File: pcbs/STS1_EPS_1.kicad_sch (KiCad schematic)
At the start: 4 parts, among them J1 Inter-EPS, U12 BD50GA5WEFJ

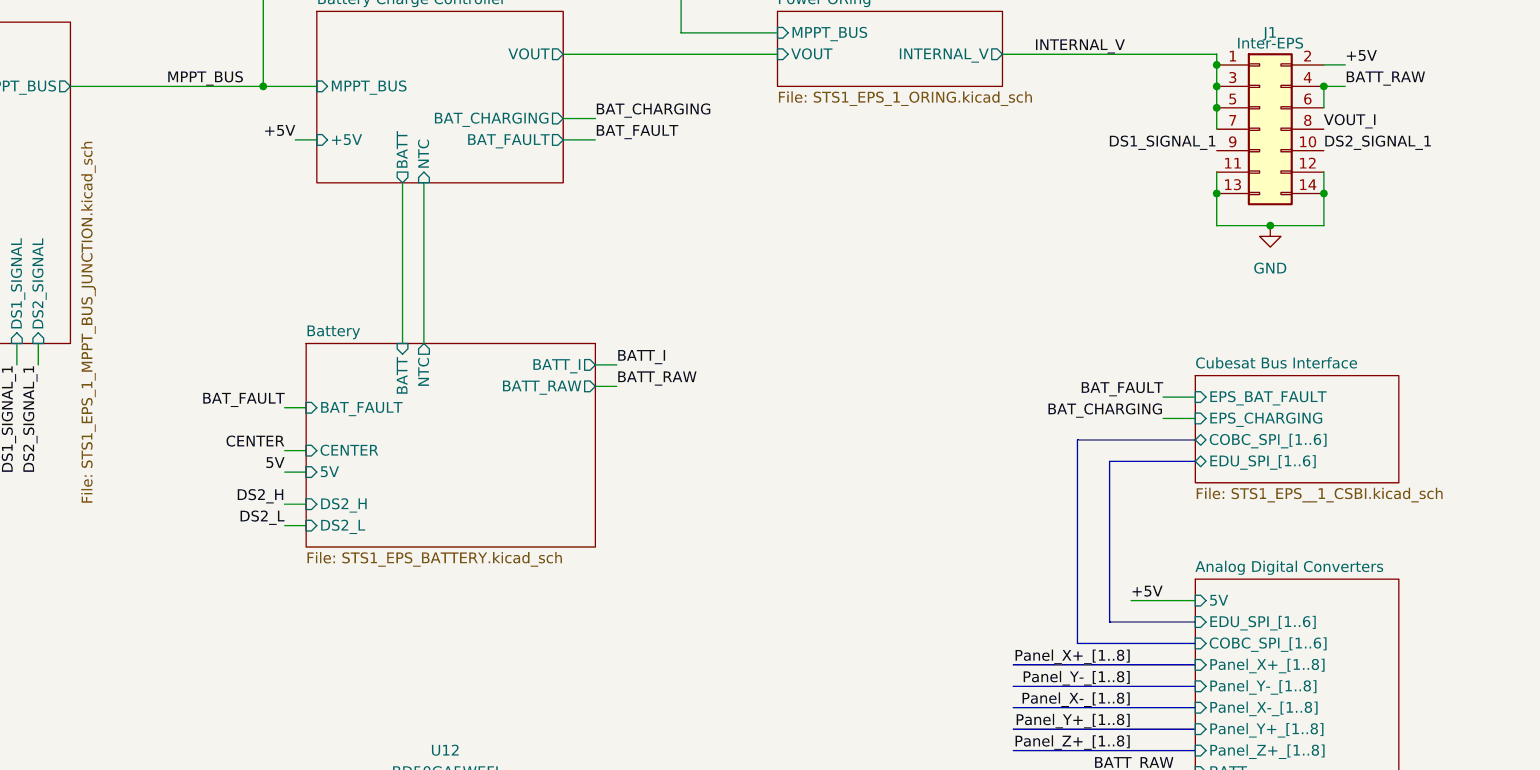
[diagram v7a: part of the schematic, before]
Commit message: Worked on STS1_EPS_2 layout.
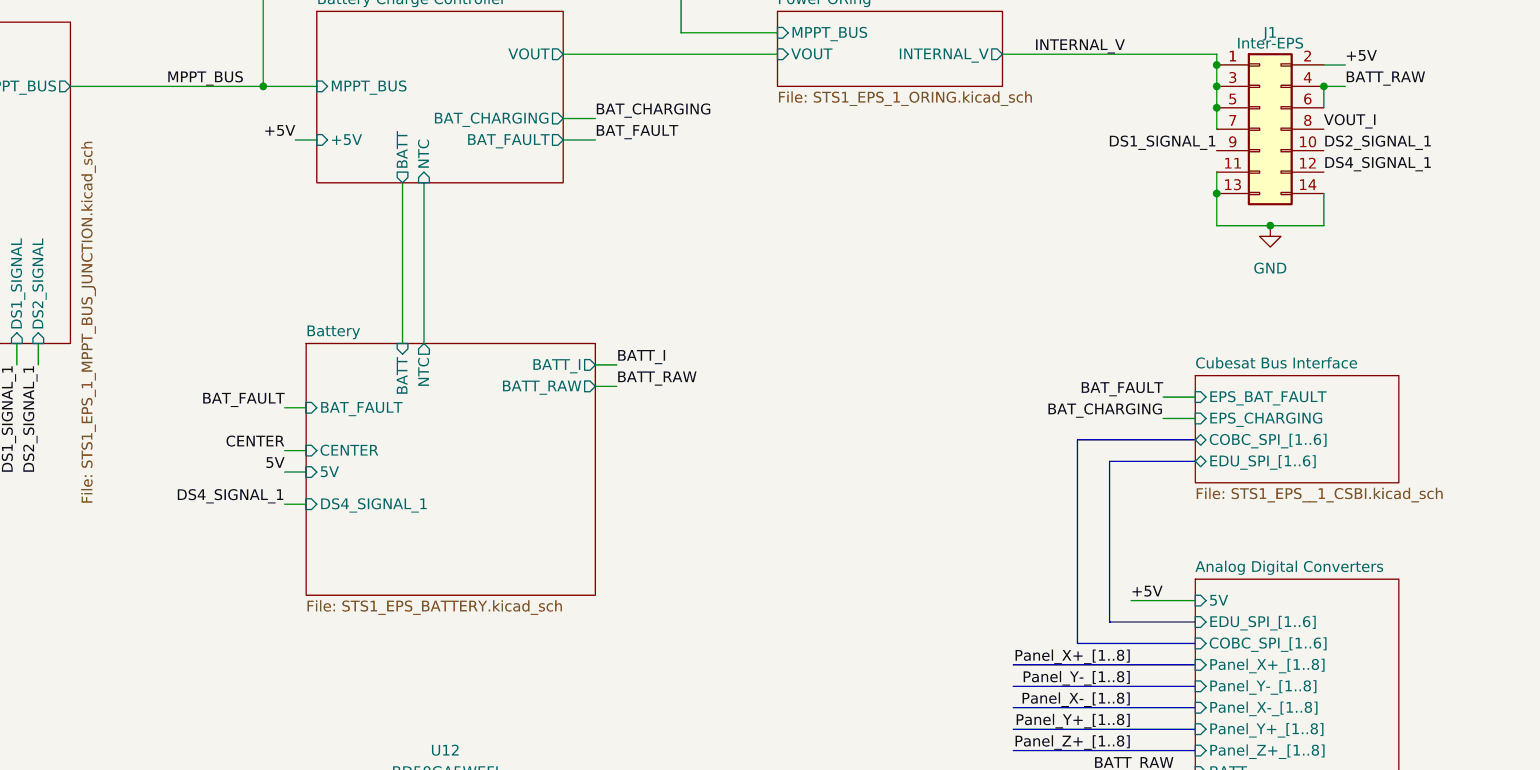
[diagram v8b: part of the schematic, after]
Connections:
- net GND: no longer J1.12 (Pin_12)
- new net DS4_SIGNAL_1: J1.12 (Pin_12)
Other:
- sheet Battery ports: added DS4_SIGNAL_1; removed DS2_H, DS2_L
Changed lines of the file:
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@@
   (junction (at 124.46 34.29) (diameter 0) (color 0 0 0 0)
-  )
-  (junction (at 250.19 46.99) (diameter 0) (color 0 0 0 0)
   )
   (junction (at 134.62 120.65) (diameter 0) (color 0 0 0 0)
@@
     (stroke (width 0) (type default) (color 0 0 0 0))
   )
-  (wire (pts (xy 250.19 44.45) (xy 250.19 46.99))
-    (stroke (width 0) (type default) (color 0 0 0 0))
-  )
   (wire (pts (xy 81.28 64.77) (xy 81.28 67.31))
     (stroke (width 0) (type default) (color 0 0 0 0))
@@
     (stroke (width 0) (type default) (color 0 0 0 0))
   )
-  (wire (pts (xy 127 86.36) (xy 129.54 86.36))
-    (stroke (width 0) (type default) (color 0 0 0 0))
-  )
   (wire (pts (xy 130.81 120.65) (xy 134.62 120.65))
     (stroke (width 0) (type default) (color 0 0 0 0))
@@
     (effects (font (size 1.27 1.27)) (justify left bottom))
   )
-  (label "DS2_L" (at 127 86.36 180)
-    (effects (font (size 1.27 1.27)) (justify right bottom))
-  )
   (label "BAT_CHARGING" (at 231.14 73.66 180)
     (effects (font (size 1.27 1.27)) (justify right bottom))
@@
     (effects (font (size 1.27 1.27)) (justify right bottom))
   )
+  (label "DS4_SIGNAL_1" (at 127 83.82 180)
+    (effects (font (size 1.27 1.27)) (justify right bottom))
+  )
   (label "Panel_Y-_[1..8]" (at 227.33 105.41 180)
     (effects (font (size 1.27 1.27)) (justify right bottom))
@@
     (effects (font (size 1.27 1.27)) (justify right bottom))
   )
+  (label "DS4_SIGNAL_1" (at 250.19 44.45 0)
+    (effects (font (size 1.27 1.27)) (justify left bottom))
+  )
   (label "MPPT_Z+_1_I" (at 232.41 140.97 180)
     (effects (font (size 1.27 1.27)) (justify right bottom))
@@
   (label "BATT_RAW" (at 166.37 69.85 0)
     (effects (font (size 1.27 1.27)) (justify left bottom))
-  )
-  (label "DS2_H" (at 127 83.82 180)
-    (effects (font (size 1.27 1.27)) (justify right bottom))
   )
   (label "MPPT_Z+_1_I" (at 86.36 67.31 270)
@@
     )
   )
-  (sheet (at 129.54 64.77) (size 34.29 24.13) (fields_autoplaced)
+  (sheet (at 129.54 64.77) (size 34.29 29.845) (fields_autoplaced)
     (stroke (width 0.1524) (type solid) (color 0 0 0 0))
     (fill (color 255 255 0 1.0000))
@@
       (effects (font (size 1.27 1.27)) (justify left bottom))
     )
-    (property "Sheet file" "STS1_EPS_BATTERY.kicad_sch" (id 1) (at 129.54 89.4846 0)
+    (property "Sheet file" "STS1_EPS_BATTERY.kicad_sch" (id 1) (at 129.54 95.1996 0)
       (effects (font (size 1.27 1.27)) (justify left top))
     )
@@
       (effects (font (size 1.27 1.27)) (justify right))
     )
-    (pin "DS2_H" input (at 129.54 83.82 180)
-      (effects (font (size 1.27 1.27)) (justify left))
-    )
-    (pin "DS2_L" input (at 129.54 86.36 180)
+    (pin "DS4_SIGNAL_1" input (at 129.54 83.82 180)
       (effects (font (size 1.27 1.27)) (justify left))
     )
@@
       (reference "#PWR048") (unit 1) (value "GND") (footprint "")
     )
-    (path "/8efe9fa1-fd79-411e-9a4d-de1a5e8757ee/5d8dcbd3-a26f-4bd9-8369-6f9912c614bf"
+    (path "/8efe9fa1-fd79-411e-9a4d-de1a5e8757ee/c0bc4476-4aa5-479f-b4a3-34a1f6026b8d"
       (reference "#PWR049") (unit 1) (value "GND") (footprint "")
     )
@@
     )
     (path "/3f2412fd-ceb3-4d5f-b693-7628adb9c64f/4e6fb95b-2fd2-4223-9ebd-6e07ed394875"
-      (reference "C8") (unit 1) (value "200n") (footprint "Capacitor_SMD:C_1812_4532Metric")
+      (reference "C8") (unit 1) (value "200n") (footprint "Capacitor_SMD:C_0805_2012Metric")
     )
     (path "/3f2412fd-ceb3-4d5f-b693-7628adb9c64f/0822b058-9658-4bd1-b4dc-a10863dac121"
@@
       (reference "Q3") (unit 1) (value "SI7135DP-T1-GE3") (footprint "STS_Package_SO:POWERPAK_SO8_single")
     )
+    (path "/8efe9fa1-fd79-411e-9a4d-de1a5e8757ee/767c2000-78a8-499c-9a48-e6fb1d04ae26"
+      (reference "Q4") (unit 1) (value "SI7272DP-T1-GE3") (footprint "STS_Package_SO:POWERPAK_SO8")
+    )
+    (path "/8efe9fa1-fd79-411e-9a4d-de1a5e8757ee/86db2731-62ec-450e-ab7c-b2796a31e495"
+      (reference "Q4") (unit 2) (value "SI7272DP-T1-GE3") (footprint "STS_Package_SO:POWERPAK_SO8")
+    )
     (path "/3f2412fd-ceb3-4d5f-b693-7628adb9c64f/78647b3a-bb18-4641-a0b7-ebe2e13283d3"
       (reference "R1") (unit 1) (value "135k") (footprint "Resistor_SMD:R_0805_2012Metric")
@@
       (reference "R37") (unit 1) (value "0") (footprint "Resistor_SMD:R_0805_2012Metric")
     )
-    (path "/8efe9fa1-fd79-411e-9a4d-de1a5e8757ee/c6c5a199-be2a-448c-82e3-9e57c4744b7c"
-      (reference "R44") (unit 1) (value "0") (footprint "Resistor_SMD:R_0805_2012Metric")
+    (path "/3f2412fd-ceb3-4d5f-b693-7628adb9c64f/162ca839-a2bd-4916-963a-6aaf38f4e25f"
+      (reference "R38") (unit 1) (value "100k") (footprint "Resistor_SMD:R_0805_2012Metric")
+    )
+    (path "/8efe9fa1-fd79-411e-9a4d-de1a5e8757ee/1684b46f-112a-4cc7-812b-7b58cca2364d"
+      (reference "R39") (unit 1) (value "1M") (footprint "Resistor_SMD:R_0805_2012Metric")
     )
     (path "/385aadbb-2cd4-43e1-9f59-43b251a5f3b9/6d5c5344-4166-4f6b-8a60-61e8e3fac33e"
       (reference "R45") (unit 1) (value "0") (footprint "Resistor_SMD:R_0805_2012Metric")
     )
-    (path "/3f2412fd-ceb3-4d5f-b693-7628adb9c64f/162ca839-a2bd-4916-963a-6aaf38f4e25f"
-      (reference "R?") (unit 1) (value "100k") (footprint "Resistor_SMD:R_0805_2012Metric")
-    )
     (path "/3f2412fd-ceb3-4d5f-b693-7628adb9c64f/f74591fa-cb68-47ad-92f1-f91edd2699b9"
       (reference "RV1") (unit 1) (value "50k") (footprint "Potentiometer_SMD:Potentiometer_Bourns_TC33X_Vertical")
@@
       (reference "U1") (unit 1) (value "LTC4020EUHFPBF") (footprint "STS_Package_DFN_QFN:AD_QFN-38_UHF")
     )
+    (path "/3f2412fd-ceb3-4d5f-b693-7628adb9c64f/dbec227c-8f41-4541-bcbe-07875e029fcf"
+      (reference "U2") (unit 1) (value "SI7272DP-T1-GE3") (footprint "STS_Package_SO:POWERPAK_SO8")
+    )
     (path "/3f2412fd-ceb3-4d5f-b693-7628adb9c64f/19646095-6b26-4483-8648-0e6783e27ac2"
-      (reference "U2") (unit 1) (value "SI7272DP-T1-GE3") (footprint "STS_Package_SO:POWERPAK_SO8")
-    )
-    (path "/3f2412fd-ceb3-4d5f-b693-7628adb9c64f/dbec227c-8f41-4541-bcbe-07875e029fcf"
       (reference "U2") (unit 2) (value "SI7272DP-T1-GE3") (footprint "STS_Package_SO:POWERPAK_SO8")
     )
+    (path "/3f2412fd-ceb3-4d5f-b693-7628adb9c64f/ebc1de83-5877-4385-ba1e-c7d8e677ab87"
+      (reference "U3") (unit 1) (value "SI7272DP-T1-GE3") (footprint "STS_Package_SO:POWERPAK_SO8")
+    )
     (path "/3f2412fd-ceb3-4d5f-b693-7628adb9c64f/cc6c4ec8-91e0-4c05-9d35-f249289df484"
-      (reference "U3") (unit 1) (value "SI7272DP-T1-GE3") (footprint "STS_Package_SO:POWERPAK_SO8")
-    )
-    (path "/3f2412fd-ceb3-4d5f-b693-7628adb9c64f/ebc1de83-5877-4385-ba1e-c7d8e677ab87"
       (reference "U3") (unit 2) (value "SI7272DP-T1-GE3") (footprint "STS_Package_SO:POWERPAK_SO8")
     )
